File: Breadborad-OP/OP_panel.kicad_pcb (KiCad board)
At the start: 2 copper layers, 30 parts, among them J1 Conn_01x04_Pin, J2 Conn_01x04_Pin, J4 Conn_01x04_Pin, U1 NE5532, U2 LM311

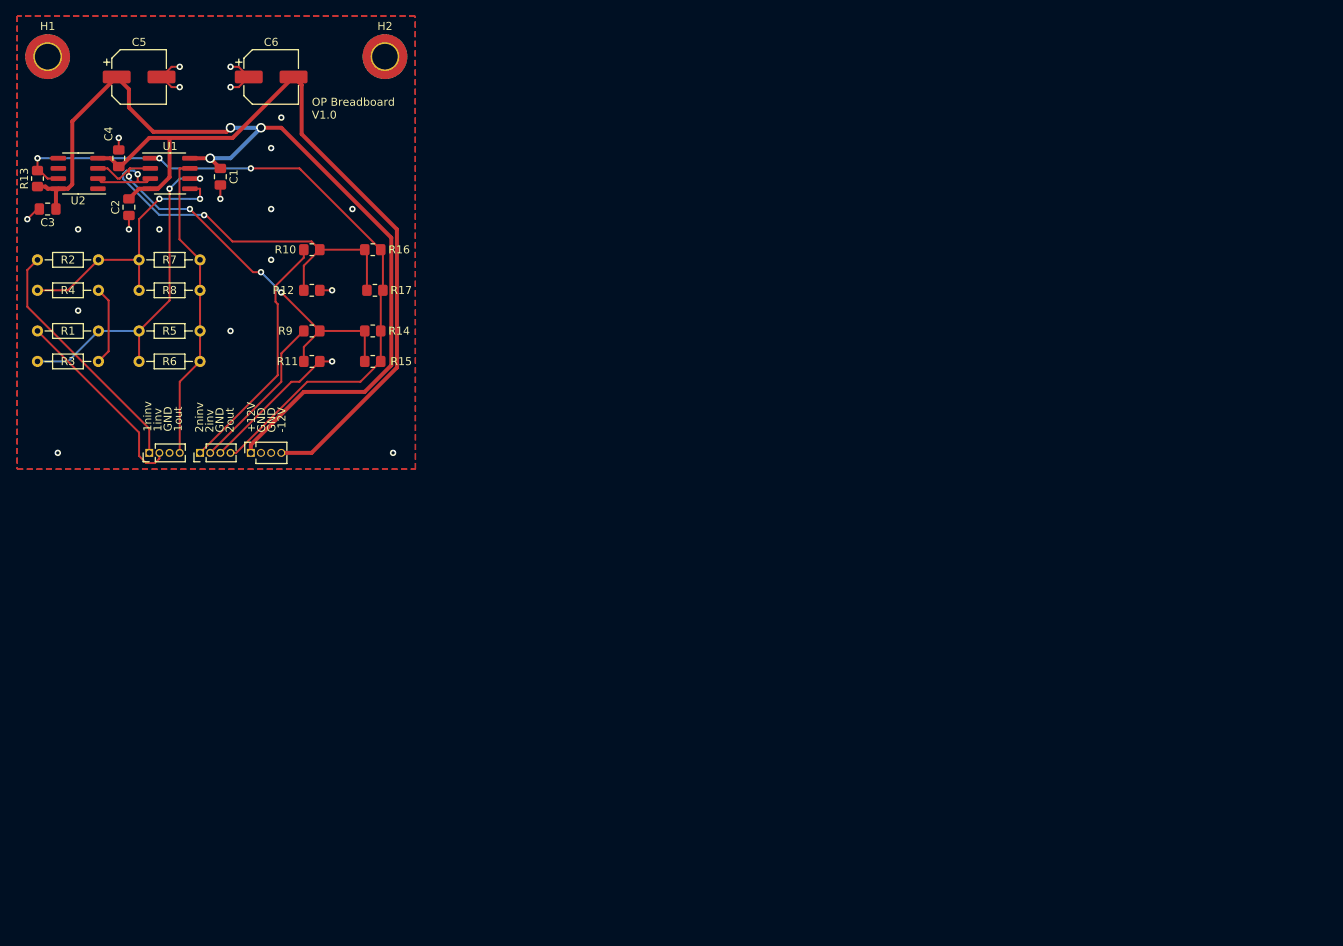
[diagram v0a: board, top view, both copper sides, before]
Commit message: Anschlussleiste auf 2,56 mm Rastermaß geändert.
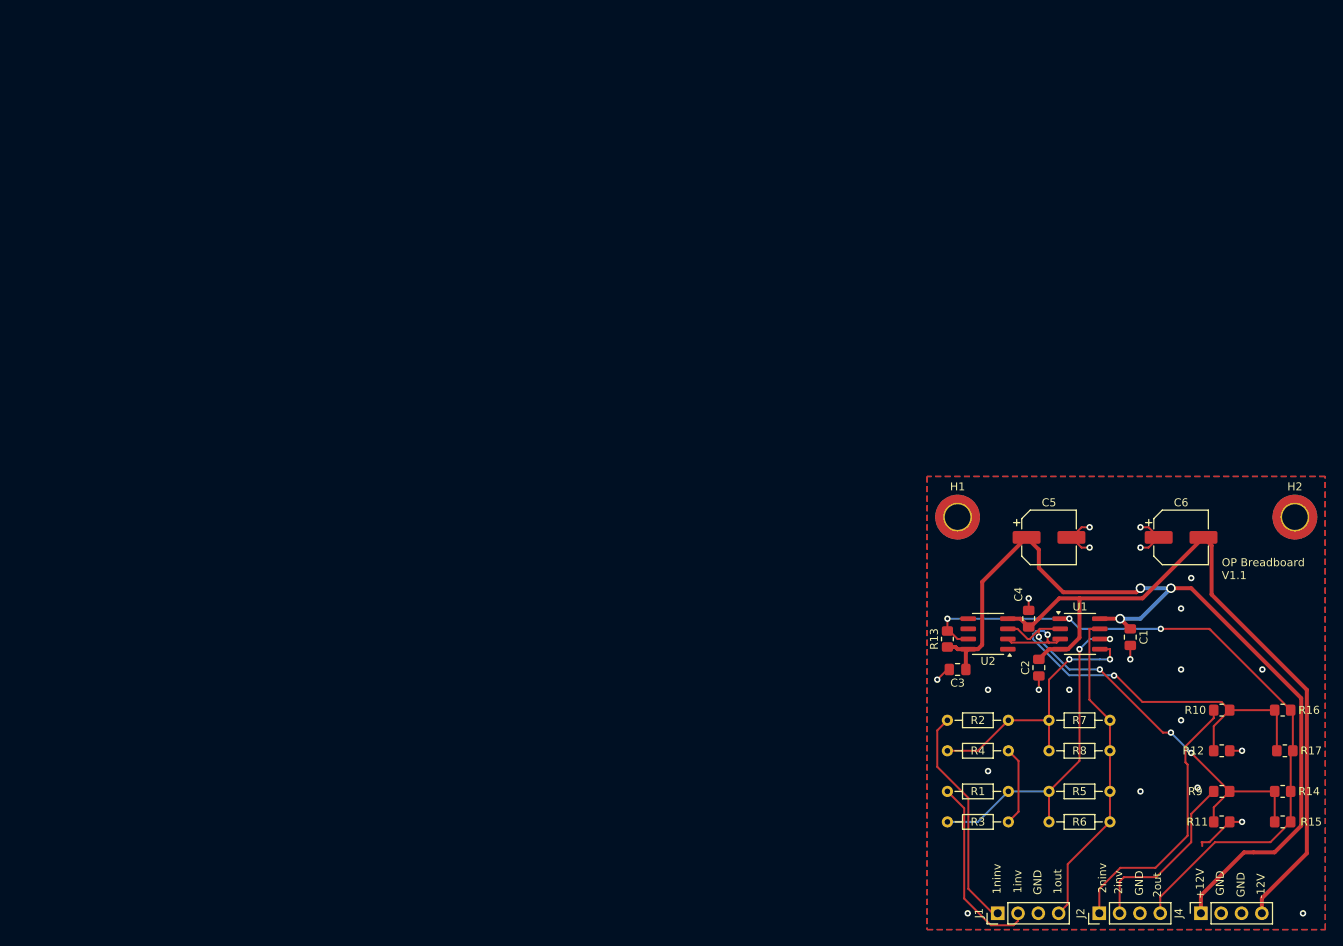
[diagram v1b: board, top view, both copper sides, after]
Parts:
- J1, J2: footprint Connector_PinHeader_1.27mm:PinHeader_1x04_P1.27mm_Vertical -> Connector_PinHeader_2.54mm:PinHeader_1x04_P2.54mm_Vertical
- J4: footprint Connector_PinSocket_1.27mm:PinSocket_1x04_P1.27mm_Vertical -> Connector_PinSocket_2.54mm:PinSocket_1x04_P2.54mm_Vertical
- moved J4 132.0 mm to (225.9, 145.0)
- moved C2 127.5 mm to (205.7, 114.3)
- moved C3 127.5 mm to (195.5, 114.5)
- moved C6 127.5 mm to (223.4, 98.0)
- moved H1 127.5 mm to (195.5, 95.5)
- moved H2 127.5 mm to (237.7, 95.5)
- moved R1 127.5 mm to (194.2, 129.8)
- moved R13 127.5 mm to (194.2, 110.7)
- moved R17 127.5 mm to (236.4, 124.7)
- moved R2 127.5 mm to (194.2, 120.9)
- moved R3 127.5 mm to (201.9, 133.6)
- moved R4 127.5 mm to (201.9, 124.7)
- moved C1 127.5 mm to (217.1, 110.5)
- moved C4 127.5 mm to (204.4, 108.2)
- moved C5 127.5 mm to (206.9, 98.0)
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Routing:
- net GND: track 48.9 -> 36.9 mm, vias 21 -> 22
- net -12V: track 101.2 -> 95.3 mm
- net +12V: track 118.4 -> 114.1 mm
- net Net-(J2-Pin_1): track 31.0 -> 34.1 mm
- net Net-(J1-Pin_1): track 31.0 -> 28.1 mm
- net Net-(J2-Pin_2): track 20.1 -> 22.5 mm
- net Net-(J1-Pin_4): track 39.0 -> 40.6 mm
- net Net-(J2-Pin_4): track 91.1 -> 89.8 mm
- net Net-(J1-Pin_2): track 24.7 -> 23.5 mm
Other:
- board text added: "OP Breadboard V1.1"
- board text removed: "OP Breadboard V1.0"
